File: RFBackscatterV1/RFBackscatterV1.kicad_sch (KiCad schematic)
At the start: 9 parts, among them J1 SMA-J-P-H-RA-TH1, U1 SIT1534AI-H4-DCC-00.001E

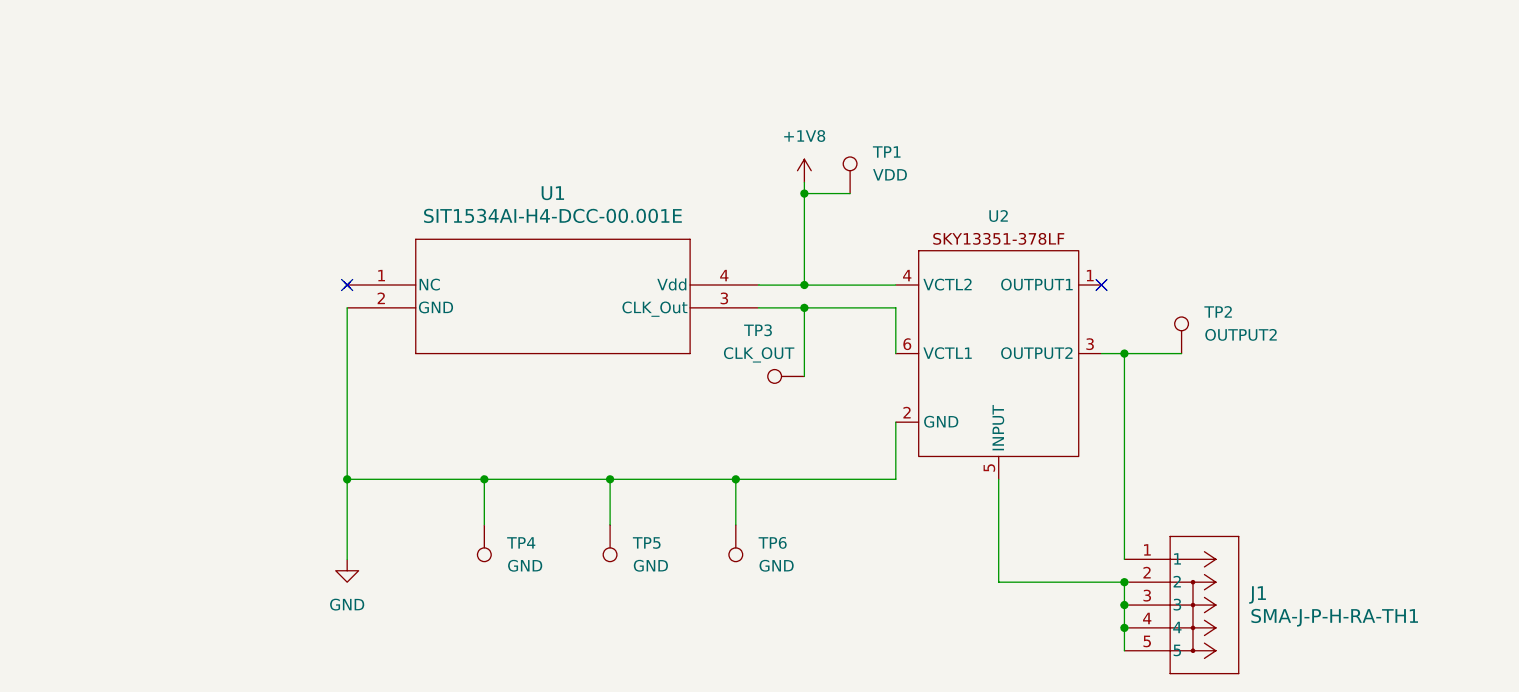
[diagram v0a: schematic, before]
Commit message: generated manufacturing files for V1.0
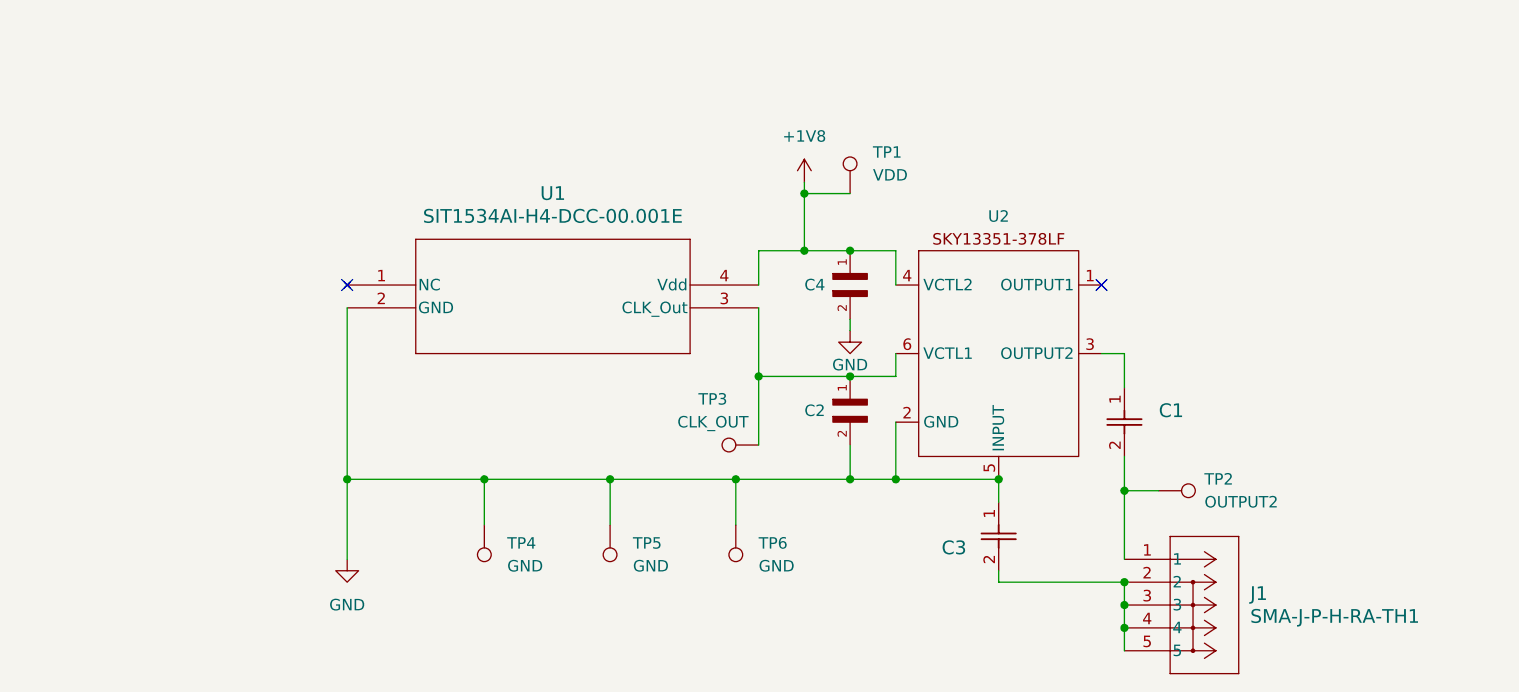
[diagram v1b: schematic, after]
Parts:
- added C1: CBR04C101J3GAC, WADARfootprints:CAPC10555_55N_KEM, symbol CBR04C101J3GAC:CBR04C101J3GAC
- added C2, C4: GJM1555C1H330JB01D, WADARfootprints:CAPC10555_55N_KEM, symbol GJM1555C1H330JB01D:GJM1555C1H330JB01D
- added C3: CBR04C101J3GAC, CAPC10555_55N_KEM, symbol CBR04C101J3GAC:CBR04C101J3GAC
- TP1, TP2, TP3, TP4, TP5, TP6: footprint TestPoint:TestPoint_Pad_2.0x2.0mm -> JLab_FP:EpicTestPointV1
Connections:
- net +1V8: now also C4.1
- net GND: now also U2.5 (INPUT), C2.2, C3.1, C4.2
- net at J1.1, TP2.1: now also C1.2; no longer U2.3 (OUTPUT2)
- net at J1.2, J1.3, J1.4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: now also C3.2; no longer U2.5 (INPUT)
- net at TP3.1, U1.3 (CLK_Out), U2.6 (VCTL1): now also C2.1
- new net: C1.1, U2.3 (OUTPUT2)
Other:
- moved on the sheet: TP2, TP3

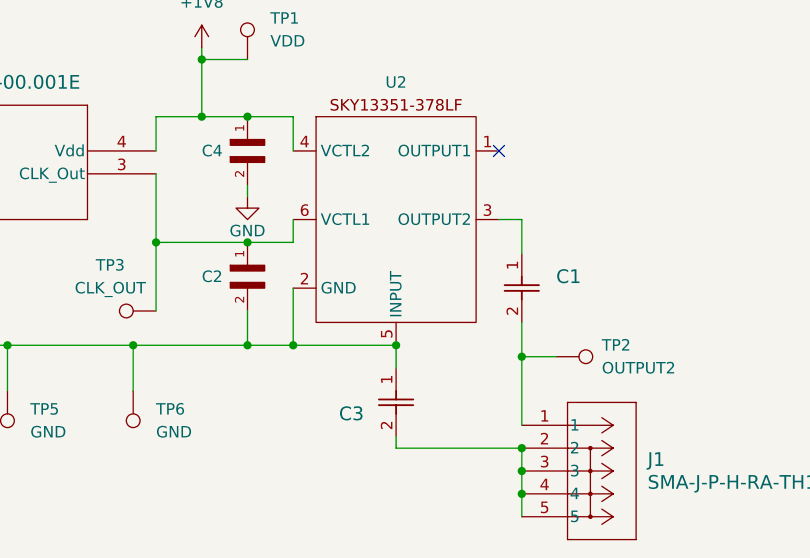
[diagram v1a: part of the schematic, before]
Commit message: fixed input pin capacitor and RF connector ground
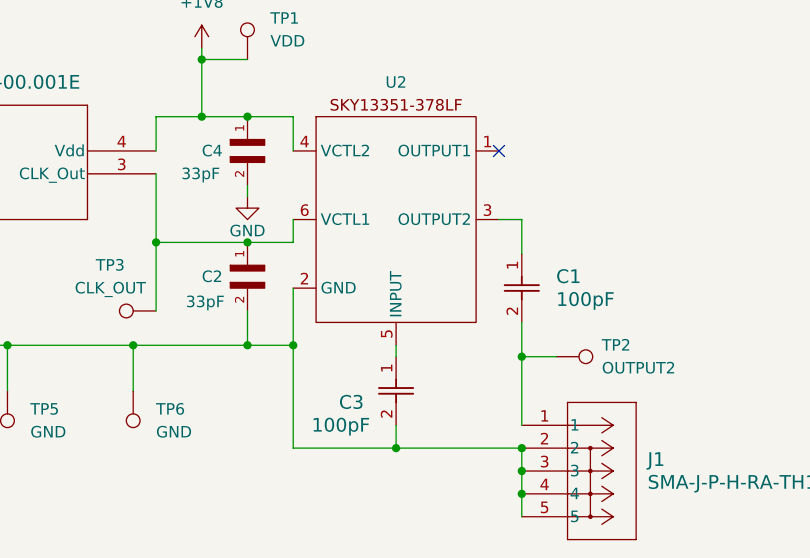
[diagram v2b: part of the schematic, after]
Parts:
- C1, C3: value CBR04C101J3GAC -> 100pF
- C2, C4: value GJM1555C1H330JB01D -> 33pF
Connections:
- net GND: now also C3.2, J1.2, J1.3, J1.4, J1.5; no longer C3.1, U2.5 (INPUT)
- new net: C3.1, U2.5 (INPUT)
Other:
- moved on the sheet: C3

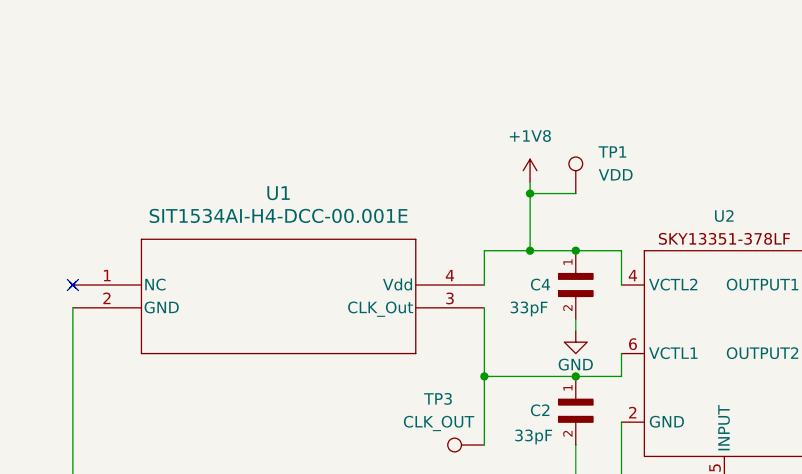
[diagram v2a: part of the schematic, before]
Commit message: 1.1 added coin cell
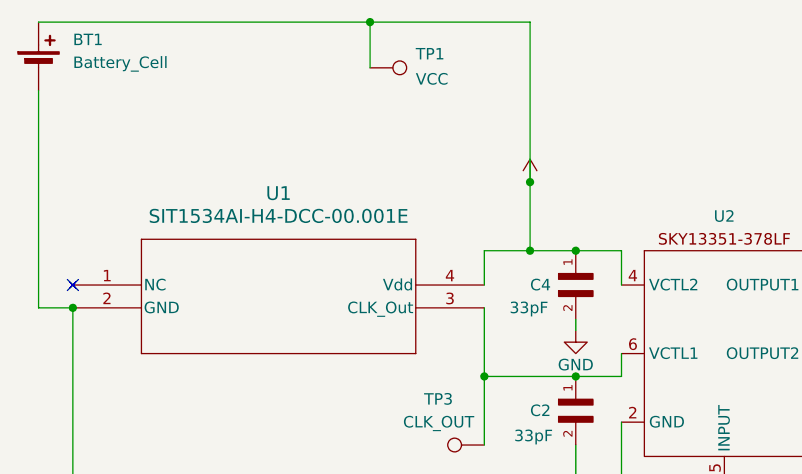
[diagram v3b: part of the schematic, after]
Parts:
- added BT1: Battery_Cell, WADARfootprints:BAT-SMD_MY-LR44-02, symbol Device:Battery_Cell
- J1: footprint CONN_SMA-J-P-H-RA-TH1_SAI -> WADARfootprints:CONN_SMA-J-P-H-RA-TH1_SAI
- TP1: value VDD -> VCC
- U1: footprint XTAL4_SiT1533_SIT -> WADARfootprints:XTAL4_SiT1533_SIT
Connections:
- net +1V8: now also BT1.1 (+)
- net GND: now also BT1.2 (-)

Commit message: alexandre's changes; schematic awaiting confirmation
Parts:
- removed C1: 100pF, WADARfootprints:CAPC10555_55N_KEM, symbol CBR04C101J3GAC:CBR04C101J3GAC
- removed TP2: OUTPUT2, JLab_FP:EpicTestPointV1, symbol Connector:TestPoint
- added R1: 50Ω, symbol Device:R
- added U3: 74LVC1GU04DRL, Package_TO_SOT_SMD:SOT-553, symbol 74xGxx:74LVC1GU04DRL
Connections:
- net +1V8: now also U3.5 (VCC); no longer C4.1, U2.4 (VCTL2)
- net GND: now also U2.1 (OUTPUT1), R1.2, U3.3 (GND); no longer C3.2
- net at U2.3 (OUTPUT2): now also R1.1
- net at J1.1: now also C3.2
- net at C2.1, TP3.1, U1.3 (CLK_Out)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: now also U3.2
- new net: C4.1, U2.4 (VCTL2), U3.4
- no-connect marks 2 -> 1
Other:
- moved on the sheet: BT1, TP1, TP3, TP4, TP5, TP6, U1

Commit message: DNP R1
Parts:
- R1: value 50Ω -> DNP
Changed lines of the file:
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@@
 			)
 		)
-		(property "Value" "50Ω"
+		(property "Value" "DNP"
 			(at 185.42 93.9799 0)
 			(effects

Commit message: PCB updated
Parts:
- removed R1: DNP, symbol Device:R
- removed TP4: GND, JLab_FP:EpicTestPointV1, symbol Connector:TestPoint
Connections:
- net GND: now also U2.3 (OUTPUT2)
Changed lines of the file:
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@@
-	)
-	(junction
-		(at 76.2 101.6)
-		(diameter 0)
-		(color 0 0 0 0)
 	)
 	(junction
@@
 	(wire
 		(pts
-			(xy 182.88 87.63) (xy 182.88 88.9)
+			(xy 182.88 87.63) (xy 182.88 99.06)
 		)
 		(stroke
@@
 	(wire
 		(pts
-			(xy 60.96 101.6) (xy 76.2 101.6)
+			(xy 60.96 101.6) (xy 90.17 101.6)
 		)
 		(stroke
@@
 	(wire
 		(pts
-			(xy 182.88 96.52) (xy 182.88 99.06)
-		)
-		(stroke
-			(width 0)
-			(type default)
-		)
-	)
-	(wire
-		(pts
 			(xy 152.4 95.25) (xy 152.4 101.6)
 		)
@@
 	(wire
 		(pts
-			(xy 76.2 101.6) (xy 90.17 101.6)
-		)
-		(stroke
-			(width 0)
-			(type default)
-		)
-	)
-	(wire
-		(pts
 			(xy 114.3 68.58) (xy 114.3 90.17)
 		)
@@
 		(pts
 			(xy 57.15 82.55) (xy 60.96 82.55)
-		)
-		(stroke
-			(width 0)
-			(type default)
-		)
-	)
-	(wire
-		(pts
-			(xy 76.2 101.6) (xy 76.2 106.68)
 		)
 		(stroke
@@
 	)
 	(symbol
-		(lib_id "Device:R")
-		(at 182.88 92.71 0)
-		(unit 1)
-		(exclude_from_sim no)
-		(in_bom yes)
-		(on_board yes)
-		(dnp no)
-		(fields_autoplaced yes)
-		(property "Reference" "R1"
-			(at 185.42 91.4399 0)
-			(effects
-				(font
-					(size 1.27 1.27)
-				)
-				(justify left)
-			)
-		)
-		(property "Value" "DNP"
-			(at 185.42 93.9799 0)
-			(effects
-				(font
-					(size 1.27 1.27)
-				)
-				(justify left)
-			)
-		)
-		(property "Footprint" ""
-			(at 181.102 92.71 90)
-			(effects
-				(font
-					(size 1.27 1.27)
-				)
-				(hide yes)
-			)
-		)
-		(property "Datasheet" "~"
-			(at 182.88 92.71 0)
-			(effects
-				(font
-					(size 1.27 1.27)
-				)
-				(hide yes)
-			)
-		)
-		(property "Description" "Resistor"
-			(at 182.88 92.71 0)
-			(effects
-				(font
-					(size 1.27 1.27)
-				)
-				(hide yes)
-			)
-		)
-		(pin "1"
-		)
-		(pin "2"
-		)
-		(instances
-			(project ""
-				(path "/1b480a55-1292-4321-8fce-0463cf94490c"
-					(reference "R1")
-					(unit 1)
-				)
-			)
-		)
-	)
-	(symbol
 		(lib_id "Connector:TestPoint")
 		(at 104.14 106.68 180)
@@
 					(unit 1)
 				)
-			)
-		)
-	)
-	(symbol
-		(lib_id "Connector:TestPoint")
-		(at 76.2 106.68 180)
-		(unit 1)
-		(exclude_from_sim no)
-		(in_bom yes)
-		(on_board yes)
-		(dnp no)
-		(fields_autoplaced yes)
-		(property "Reference" "TP4"
-			(at 78.74 108.712 0)
-			(effects
-				(font
-					(size 1.27 1.27)
-				)
-				(justify right)
-			)
-		)
-		(property "Value" "GND"
-			(at 78.74 111.252 0)
-			(effects
-				(font
-					(size 1.27 1.27)
-				)
-				(justify right)
-			)
-		)
-		(property "Footprint" "JLab_FP:EpicTestPointV1"
-			(at 71.12 106.68 0)
-			(effects
-				(font
-					(size 1.27 1.27)
-				)
-				(hide yes)
-			)
-		)
-		(property "Datasheet" "  (layer \"F.Cu\")"
-			(at 71.12 106.68 0)
-			(effects
-				(font
-					(size 1.27 1.27)
-				)
-				(hide yes)
-			)
-		)
-		(property "Description" ""
-			(at 76.2 106.68 0)
-			(effects
-				(font
-					(size 1.27 1.27)
-				)
-				(hide yes)
-			)
-		)
-		(pin "1"
-		)
-		(instances
-			(project "RFBackscatterV1"
-				(path "/1b480a55-1292-4321-8fce-0463cf94490c"
-					(reference "TP4")
-					(unit 1)
-				)

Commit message: alexandre's advice pt2
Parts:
- added C1, C5: 10nF, Capacitor_SMD:C_0402_1005Metric, symbol CBR04C101J3GAC:CBR04C101J3GAC
- added R1: DNP, symbol Device:R
- BT1: footprint WADARfootprints:BAT-SMD_MY-LR44-02 -> Battery:BatteryHolder_Keystone_1060_1x2032
- C3: value 100pF -> 10nF; footprint CAPC10555_55N_KEM -> Capacitor_SMD:C_0402_1005Metric
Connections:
- net GND: now also C5.2, R1.2; no longer U2.1 (OUTPUT1), U2.3 (OUTPUT2)
- net +1V8 renamed 3V0
- new net: C5.1, U2.1 (OUTPUT1)
- new net: C1.1, U2.3 (OUTPUT2)
- new net: C1.2, R1.1
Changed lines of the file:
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@@
-	(wire
-		(pts
-			(xy 182.88 87.63) (xy 182.88 99.06)
-		)
-		(stroke
-			(width 0)
-			(type default)
-		)
-	)
 	(wire
 		(pts
@@
 	(wire
 		(pts
+			(xy 175.26 80.01) (xy 180.34 80.01)
+		)
+		(stroke
+			(width 0)
+			(type default)
+		)
+	)
+	(wire
+		(pts
 			(xy 152.4 87.63) (xy 152.4 90.17)
 		)
@@
 	(wire
 		(pts
-			(xy 175.26 87.63) (xy 182.88 87.63)
+			(xy 187.96 80.01) (xy 190.5 80.01)
+		)
+		(stroke
+			(width 0)
+			(type default)
+		)
+	)
+	(wire
+		(pts
+			(xy 182.88 97.79) (xy 182.88 99.06)
 		)
 		(stroke
@@
 	(wire
 		(pts
-			(xy 175.26 80.01) (xy 190.5 80.01)
+			(xy 182.88 87.63) (xy 182.88 90.17)
 		)
 		(stroke
@@
 			)
 		)
-		(property "Value" "100pF"
+		(property "Value" "10nF"
 			(at 154.432 110.49 90)
 			(effects
@@
 			)
 		)
-		(property "Footprint" "CAPC10555_55N_KEM"
+		(property "Footprint" "Capacitor_SMD:C_0402_1005Metric"
 			(at 163.83 102.87 0)
 			(effects
@@
 			)
 		)
-		(property "Datasheet" "CBR04C101J3GAC"
+		(property "Datasheet" "CC0402KRX7R6BB103"
 			(at 163.83 102.87 0)
 			(effects
@@
 				(path "/1b480a55-1292-4321-8fce-0463cf94490c"
 					(reference "C3")
+					(unit 1)
+				)
+			)
+		)
+	)
+	(symbol
+		(lib_id "CBR04C101J3GAC:CBR04C101J3GAC")
+		(at 180.34 80.01 0)
+		(unit 1)
+		(exclude_from_sim no)
+		(in_bom yes)
+		(on_board yes)
+		(dnp no)
+		(property "Reference" "C5"
+			(at 180.594 82.296 0)
+			(effects
+				(font
+					(size 1.524 1.524)
+				)
+				(justify left)
+			)
+		)
+		(property "Value" "10nF"
+			(at 179.578 84.328 0)
+			(effects
+				(font
+					(size 1.524 1.524)
+				)
+				(justify left)
+			)
+		)
+		(property "Footprint" "Capacitor_SMD:C_0402_1005Metric"
+			(at 180.34 80.01 0)
+			(effects
+				(font
+					(size 1.27 1.27)
+					(italic yes)
+				)
+				(hide yes)
+			)
+		)
+		(property "Datasheet" "CC0402KRX7R6BB103"
+			(at 180.34 80.01 0)
+			(effects
+				(font
+					(size 1.27 1.27)
+					(italic yes)
+				)
+				(hide yes)
+			)
+		)
+		(property "Description" ""
+			(at 180.34 80.01 0)
+			(effects
+				(font
+					(size 1.27 1.27)
+				)
+				(hide yes)
+			)
+		)
+		(pin "1"
+		)
+		(pin "2"
+		)
+		(instances
+			(project "RFBackscatterV1"
+				(path "/1b480a55-1292-4321-8fce-0463cf94490c"
+					(reference "C5")
 					(unit 1)
 				)
@@
 	)
 	(symbol
+		(lib_id "CBR04C101J3GAC:CBR04C101J3GAC")
+		(at 175.26 87.63 0)
+		(unit 1)
+		(exclude_from_sim no)
+		(in_bom yes)
+		(on_board yes)
+		(dnp no)
+		(property "Reference" "C1"
+			(at 175.514 89.916 0)
+			(effects
+				(font
+					(size 1.524 1.524)
+				)
+				(justify left)
+			)
+		)
+		(property "Value" "10nF"
+			(at 174.498 91.948 0)
+			(effects
+				(font
+					(size 1.524 1.524)
+				)
+				(justify left)
+			)
+		)
+		(property "Footprint" "Capacitor_SMD:C_0402_1005Metric"
+			(at 175.26 87.63 0)
+			(effects
+				(font
+					(size 1.27 1.27)
+					(italic yes)
+				)
+				(hide yes)
+			)
+		)
+		(property "Datasheet" "CC0402KRX7R6BB103"
+			(at 175.26 87.63 0)
+			(effects
+				(font
+					(size 1.27 1.27)
+					(italic yes)
+				)
+				(hide yes)
+			)
+		)
+		(property "Description" ""
+			(at 175.26 87.63 0)
+			(effects
+				(font
+					(size 1.27 1.27)
+				)
+				(hide yes)
+			)
+		)
+		(pin "1"
+		)
+		(pin "2"
+		)
+		(instances
+			(project "RFBackscatterV1"
+				(path "/1b480a55-1292-4321-8fce-0463cf94490c"
+					(reference "C1")
+					(unit 1)
+				)
+			)
+		)
+	)
+	(symbol
 		(lib_id "GJM1555C1H330JB01D:GJM1555C1H330JB01D")
 		(at 147.32 92.71 270)
@@
 			)
 		)
-		(property "Footprint" "WADARfootprints:BAT-SMD_MY-LR44-02"
+		(property "Footprint" "Battery:BatteryHolder_Keystone_1060_1x2032"
 			(at 57.15 54.356 90)
 			(effects
@@
 	)
 	(symbol
+		(lib_id "Device:R")
+		(at 182.88 93.98 0)
+		(unit 1)
+		(exclude_from_sim no)
+		(in_bom yes)
+		(on_board yes)
+		(dnp yes)
+		(fields_autoplaced yes)
+		(property "Reference" "R1"
+			(at 185.42 92.7099 0)
+			(effects
+				(font
+					(size 1.27 1.27)
+				)
+				(justify left)
+			)
+		)
+		(property "Value" "DNP"
+			(at 185.42 95.2499 0)
+			(effects
+				(font
+					(size 1.27 1.27)
+				)
+				(justify left)
+			)
+		)
+		(property "Footprint" ""
+			(at 181.102 93.98 90)
+			(effects
+				(font
+					(size 1.27 1.27)
+				)
+				(hide yes)
+			)
+		)
+		(property "Datasheet" "~"
+			(at 182.88 93.98 0)
+			(effects
+				(font
+					(size 1.27 1.27)
+				)
+				(hide yes)
+			)
+		)
+		(property "Description" "Resistor"
+			(at 182.88 93.98 0)
+			(effects
+				(font
+					(size 1.27 1.27)
+				)
+				(hide yes)
+			)
+		)
+		(pin "1"
+		)
+		(pin "2"
+		)
+		(instances
+			(project ""
+				(path "/1b480a55-1292-4321-8fce-0463cf94490c"
+					(reference "R1")
+					(unit 1)
+				)
+			)
+		)
+	)
+	(symbol
 		(lib_id "Connector:TestPoint")
 		(at 106.68 97.79 90)
@@
 			)
 		)
-		(property "Value" "+1V8"
+		(property "Value" "3V0"
 			(at 123.19 57.15 0)
 			(effects

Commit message: pre-board review
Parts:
- C1: now not fitted
- C2, C4: footprint WADARfootprints:CAPC10555_55N_KEM -> Capacitor_SMD:C_0402_1005Metric
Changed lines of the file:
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@@
 			)
 		)
-		(property "Footprint" "WADARfootprints:CAPC10555_55N_KEM"
+		(property "Footprint" "Capacitor_SMD:C_0402_1005Metric"
 			(at 147.32 78.74 0)
 			(effects
@@
 			)
 		)
-		(property "Description" "GJM1555C1H330JB01D"
+		(property "Description" "0402CG330J500NT"
 			(at 147.32 78.74 0)
 			(effects
@@
 		(in_bom yes)
 		(on_board yes)
-		(dnp no)
+		(dnp yes)
 		(property "Reference" "C1"
 			(at 175.514 89.916 0)
@@
 			)
 		)
-		(property "Footprint" "WADARfootprints:CAPC10555_55N_KEM"
+		(property "Footprint" "Capacitor_SMD:C_0402_1005Metric"
 			(at 147.32 92.71 0)
 			(effects
@@
 			)
 		)
-		(property "Description" "GJM1555C1H330JB01D"
+		(property "Description" "0402CG330J500NT"
 			(at 147.32 92.71 0)
 			(effects
